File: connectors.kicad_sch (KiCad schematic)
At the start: 5 parts, among them J4 JST_VH_B2P_3.96mm, J5 JST_VH_B2P_3.96mm, J6 JST_VH_B2P_3.96mm, J7 CE, J8 CE

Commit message: First layout
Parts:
- removed J6: JST_VH_B2P_3.96mm, Connector_JST:JST_VH_B2P-VH_1x02_P3.96mm_Vertical, symbol Connector:Conn_01x02_Socket
- added H7, H8, H9: MountingHole_Pad, MountingHole:MountingHole_3.2mm_M3_DIN965_Pad_TopBottom, symbol Mechanical:MountingHole_Pad
- added J1: CE, Connector_PinHeader_2.54mm:PinHeader_1x02_P2.54mm_Vertical, symbol Connector:Conn_01x02_Pin
- added J2: LDO_EN, Connector_PinHeader_2.54mm:PinHeader_1x02_P2.54mm_Vertical, symbol Connector:Conn_01x02_Pin
- added J3: Conn_01x05_Pin, Connector_PinHeader_2.54mm:PinHeader_1x05_P2.54mm_Vertical, symbol Connector:Conn_01x05_Pin
- J7: value CE -> Thermistor_1
- J8: value CE -> Thermistor_2
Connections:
- net GND: now also H7.1, H9.1, J1.2 (Pin_2), J3.5 (Pin_5)
- new net CE_N: J1.1 (Pin_1)
- new net LDO_IN: J2.2 (Pin_2)
- new net REGN: J2.1 (Pin_1)
- new net RST: J3.4 (Pin_4)
- new net SWCLK: J3.3 (Pin_3)
- new net SWDIO: J3.2 (Pin_2)
- new net VCC: J3.1 (Pin_1)
- no-connect marks 0 -> 1
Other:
- moved on the sheet: J4, J5, J7, J8

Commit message: Fix ERC
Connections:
- net REGN renamed REGN_5V

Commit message: All connectors are deemed the same in BOM. Re-push.
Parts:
- J4, J5: MPN (none) -> TBD
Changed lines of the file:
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@@
+			)
+		)
+		(property "MPN" "TBD"
+			(at 185.42 63.5 0)
+			(effects
+				(font
+					(size 1.27 1.27)
+				)
+				(hide yes)
 			)
 		)
@@
 			(at 185.42 45.72 0)
 			(effects
+				(font
+					(size 1.27 1.27)
+				)
+				(hide yes)
+			)
+		)
+		(property "MPN" "TBD"
+			(at 185.42 45.72 0)
+			(effects

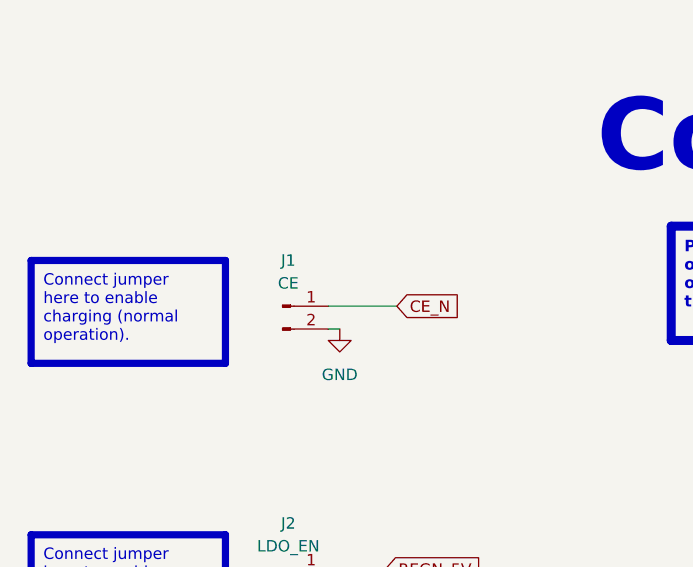
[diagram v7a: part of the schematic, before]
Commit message: Change J1 value to fix BOM
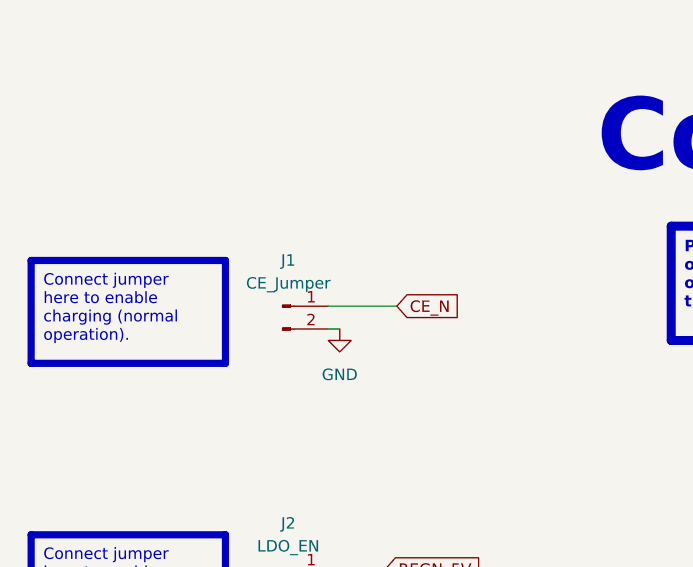
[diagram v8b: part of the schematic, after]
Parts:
- J1: value CE -> CE_Jumper
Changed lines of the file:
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@@
 			)
 		)
-		(property "Value" "CE"
+		(property "Value" "CE_Jumper"
 			(at 76.835 45.72 0)
 			(effects
